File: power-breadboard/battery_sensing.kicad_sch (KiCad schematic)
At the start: 6 parts, among them J6 JST PH, J7 JST PH, U7 DS2484R

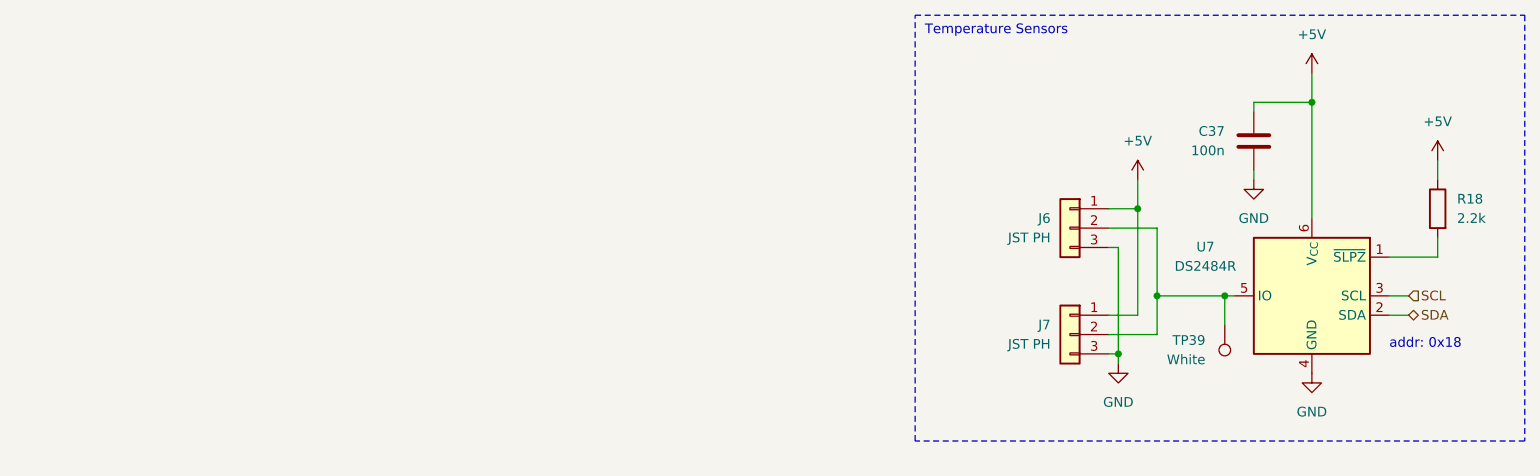
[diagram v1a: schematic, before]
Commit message: power-breadboard: finish battery temp. sensing
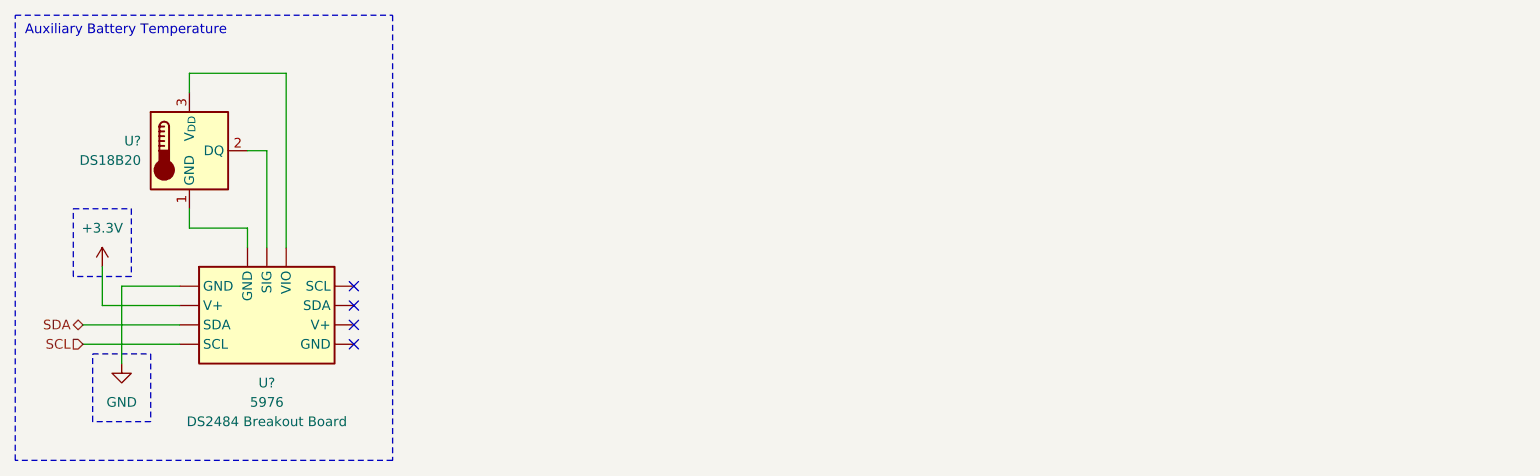
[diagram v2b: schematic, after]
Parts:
- removed C37: 100n, Capacitor_SMD:C_0402_1005Metric_Pad0.74x0.62mm_HandSolder, symbol Device:C
- removed J6, J7: JST PH, Connector_JST:JST_PH_S3B-PH-K_1x03_P2.00mm_Horizontal, symbol Connector_Generic:Conn_01x03
- removed R18: 2.2k, Resistor_SMD:R_0603_1608Metric_Pad0.98x0.95mm_HandSolder, symbol Device:R
- removed TP39: White, TestPoint:TestPoint_Keystone_5005-5009_Compact, symbol Connector:TestPoint
- removed U7: DS2484R, Package_TO_SOT_SMD:SOT-23-6, symbol Interface_Expansion:DS2484R
- added U?: 5976, symbol Exocet:Adafruit_5976
- added U?: DS18B20, Package_TO_SOT_THT:TO-92_Inline, symbol Sensor_Temperature:DS18B20
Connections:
- net GND: now also U?. (GND)
- net SCL: now also U?. (GND)
- net SDA: now also U?. (GND)
- new net: U?. (GND), U?.1 (GND)
- new net: U?. (GND), U?.2 (DQ)
- new net: U?. (GND), U?.3 (V_{DD})
- new net +3.3V: U?. (GND)
- no-connect marks 0 -> 4
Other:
- note added: "Auxiliary Battery Temperature"
- note removed: "Temperature Sensors"
- note removed: "addr: 0x18"
